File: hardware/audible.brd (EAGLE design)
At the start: 27.7 x 23.4 mm, 28 parts, among them IC1 LTC1966CMS8, J1 SQUALL_HEADER, J5 TC2030-JLINK-NL, Q1 FK3503010L, U1 MAX417ESA+, U2 MAX417ESA+

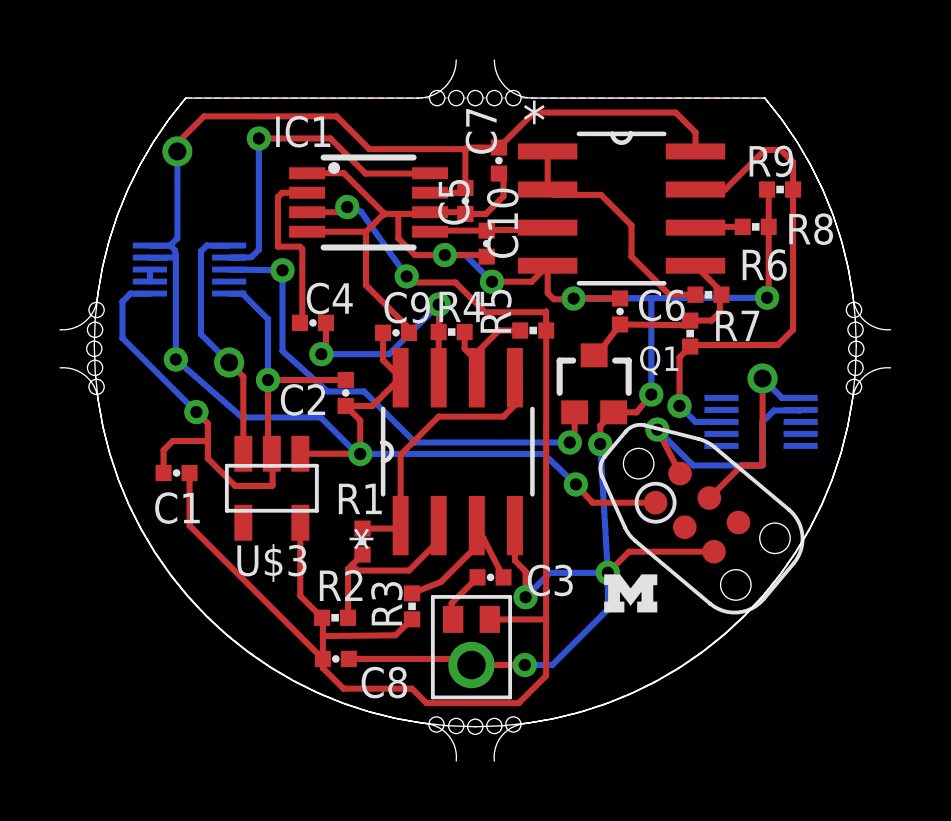
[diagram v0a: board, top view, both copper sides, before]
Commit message: Cleaned up routes all over
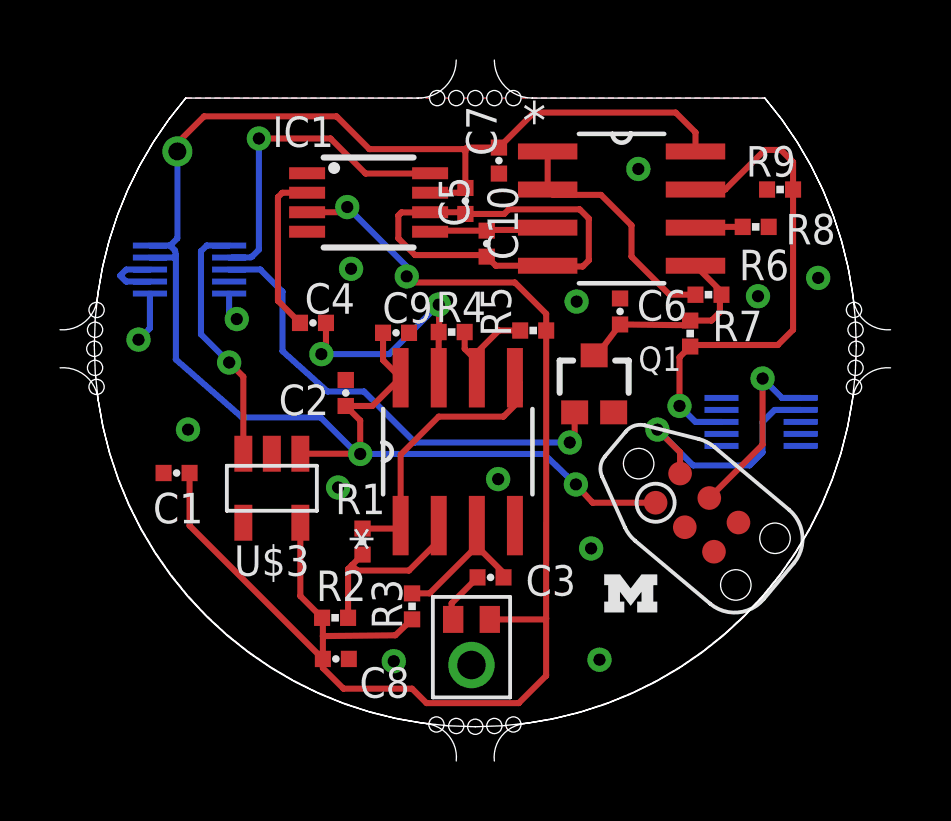
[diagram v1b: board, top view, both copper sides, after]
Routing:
- net GND: track 89.4 -> 19.2 mm, vias 11 -> 13
- net 5V: track 0.40 -> 2.15 mm
- net P24: track 16.3 -> 15.9 mm, vias 2 -> 1
- net VCC: vias 4 -> 3

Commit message: Fixed ref names
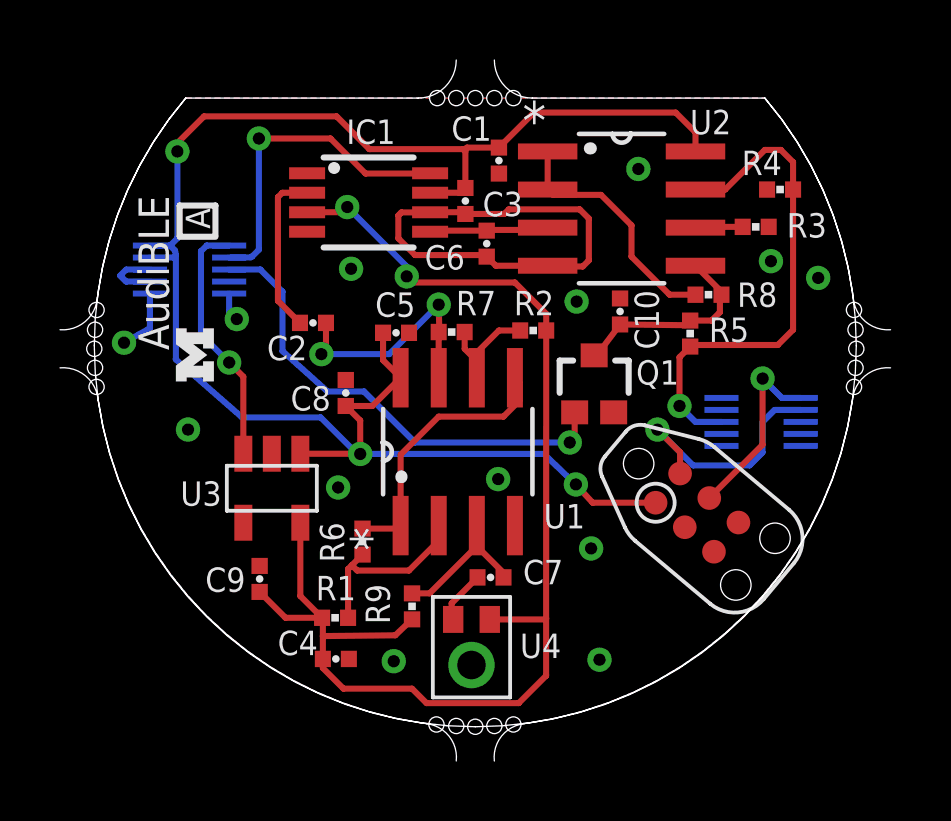
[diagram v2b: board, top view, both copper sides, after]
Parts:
- C1: value 1uF -> 0.01uF
- C10: value 0.1uF -> 22uF
- C2: value 1uF -> 100n
- C3: value 1uF -> 0.1uF
- C4: value 100n -> 0.1uF
- C5: value 1u -> 0.1uF
- C6: value 22uF -> 1u
- C7: value 0.01uF -> 1uF
- C8, C9: value 0.1uF -> 1uF
- R1: value 14k -> 1k
- R3: value 47k -> 10k
- R4: value 14k -> 10k
- R5: value 1k -> 10k
- R6: value 20k -> 14k
- R7: value 10k -> 14k
- R8: value 10k -> 20k
- R9: value 10k -> 47k
- moved R9 18.5 mm to (22.0, 4.01), turned to 90 degrees
- moved R3 17.1 mm to (33.5, 16.7), turned to 0 degrees
- moved U$1 16.6 mm to (14.8, 12.4), turned to 90 degrees
- moved C1 15.0 mm to (24.9, 18.9), turned to 90 degrees
- moved R6 14.2 mm to (20.4, 6.17), turned to 90 degrees
- moved C7 13.9 mm to (24.6, 4.98), turned to 0 degrees
- moved C3 12.6 mm to (23.8, 17.5), turned to 90 degrees
- moved R4 11.9 mm to (34.3, 17.9), turned to 180 degrees
- moved R2 11.6 mm to (26.1, 13.2)
- moved C4 11.2 mm to (19.5, 2.26), turned to 0 degrees
- moved C9 9.38 mm to (16.9, 4.93), turned to 90 degrees
- moved C8 8.87 mm to (19.8, 11.1), turned to 90 degrees
- moved R7 7.95 mm to (23.3, 13.2), turned to 0 degrees
- moved C10 6.34 mm to (29.0, 13.8), turned to 270 degrees
- moved R5 5.23 mm to (31.3, 13.1), turned to 270 degrees
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- renumbered U$2 to U4, U$3 to U3
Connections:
- net A7: now also R4.1, R5.2; no longer R7.2, R9.1
- net GND: now also C1.1, C3.1, C4.2, C9.2, R3.2, R4.2; no longer C1.2, C2.2, C7.1, C9.1, R8.2, R9.2
- net MIC: now also C7.1; no longer C3.1
- net MIC_AMP_1: now also R6.2; no longer R1.2
- net MIC_AMP_2: now also C2.1, R7.1; no longer C4.1, R4.1
- net N$1: now also C7.2, R9.2; no longer C3.2, R3.2
- net N$10: now also C10.2, R5.1, R8.2; no longer C6.2, R6.2, R7.1
- net N$2: now also C2.2; no longer C4.2
- net N$3: now also C6.2; no longer C5.2
- net N$4: now also R1.2, R6.1; no longer R1.1, R2.2
- net N$5: now also R2.1, R7.2; no longer R4.2, R5.1
- net N$6: now also R3.1; no longer R8.1
- net RMS_BUF: now also R8.1; no longer R6.1
- net VCC: now also C1.2, C3.2, C5.2, C8.1; no longer C10.2, C2.1, C7.2, C9.2
- net VREF: now also C4.1, C9.1, R1.1, R2.2, R9.1; no longer C1.1, C8.1, R2.1, R3.1, R5.2
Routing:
- net VREF: track 48.5 -> 42.9 mm
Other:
- board text added: "2016/08/12"
- board text added: "A"
- board text added: "Amit Shah"
- board text added: "AudiBLE"
- board text added: "U1"
- board text added: "U2"
- board text added: "U4"
